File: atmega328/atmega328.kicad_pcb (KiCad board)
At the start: 2 copper layers, 11 parts, among them SW201 default_switch, SW202 default_switch, U201 HEADER_3x2, U202 ATmega328-A, Y201 Crystal_GND2

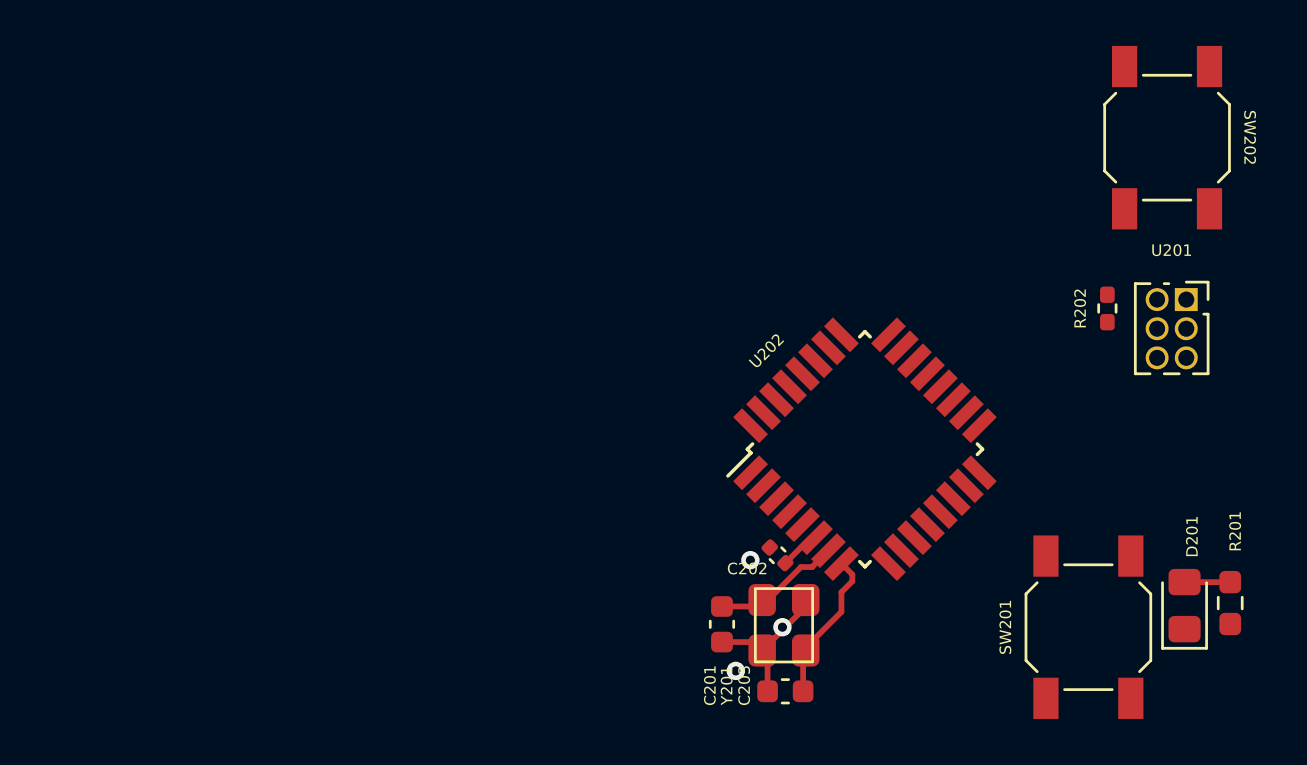
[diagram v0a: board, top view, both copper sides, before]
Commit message: made some hierarchial label changes and updated atmega328
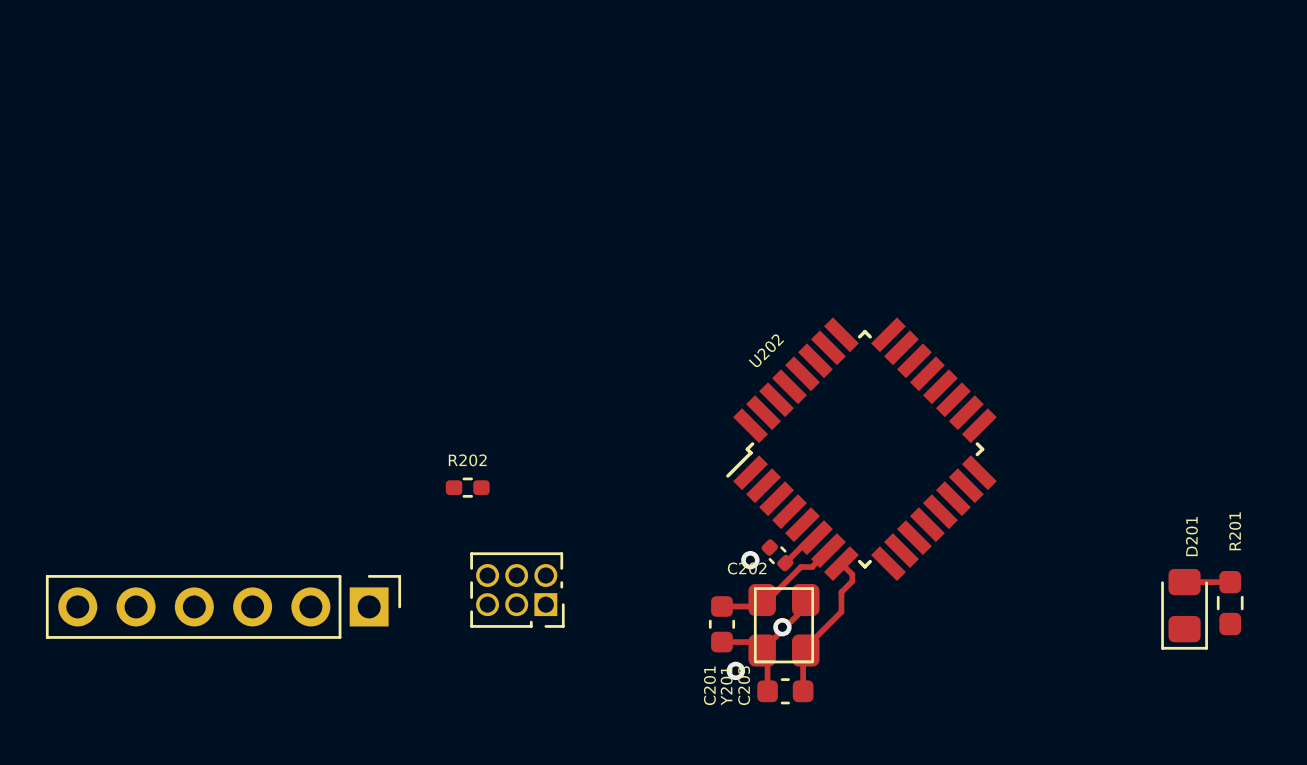
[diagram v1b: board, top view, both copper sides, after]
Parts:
- removed SW201, SW202: default_switch, custom_kicad_lib_sk:default_switch
- removed U201: HEADER_3x2, Connector_PinSocket_1.27mm:PinSocket_2x03_P1.27mm_Vertical
- added J201: HEADER_3x2, Connector_PinSocket_1.27mm:PinSocket_2x03_P1.27mm_Vertical, F.Cu at (123.8, 104.3)
- added J202: ICSP, Connector_PinHeader_2.54mm:PinHeader_1x06_P2.54mm_Vertical, F.Cu at (116.1, 104.4)
- moved R202 28.9 mm to (120.4, 99.2), turned to 0 degrees
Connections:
- net /5V renamed +5V
- net /reset renamed /Reset
